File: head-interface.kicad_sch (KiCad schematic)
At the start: 10 parts, among them J1 NOZ, J2 FANS, J3 MOTOR_IN, J4 THERM, J5 HEATER, J6 PART_FAN, J7 FAN, J8 MOTOR

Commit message: rc1
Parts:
- H1, H2: symbol Mechanical:MountingHole -> Mechanical:MountingHole_Pad
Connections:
- new net GND: H1.1, H2.1
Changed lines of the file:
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@@
 (kicad_sch (version 20211123) (generator eeschema)
   (paper "A4")
+  (wire (pts (xy 139.7 83.82) (xy 139.7 81.28))
+    (stroke (width 0) (type default) (color 0 0 0 0))
+  )
   (wire (pts (xy 67.31 78.74) (xy 67.31 82.55))
     (stroke (width 0) (type default) (color 0 0 0 0))
@@
   )
   (wire (pts (xy 62.23 71.12) (xy 62.23 78.74))
+    (stroke (width 0) (type default) (color 0 0 0 0))
+  )
+  (wire (pts (xy 48.26 85.09) (xy 48.26 81.28))
     (stroke (width 0) (type default) (color 0 0 0 0))
   )
@@
     (pin "4")
   )
+  (symbol (lib_id "power:GND") (at 48.26 85.09 0) (unit 1)
+    (in_bom yes) (on_board yes) (fields_autoplaced)
+    (property "Reference" "#PWR?" (id 0) (at 48.26 91.44 0)
+      (effects (font (size 1.27 1.27)) hide)
+    )
+    (property "Value" "GND" (id 1) (at 48.26 90.17 0))
+    (property "Footprint" "" (id 2) (at 48.26 85.09 0)
+      (effects (font (size 1.27 1.27)) hide)
+    )
+    (property "Datasheet" "" (id 3) (at 48.26 85.09 0)
+      (effects (font (size 1.27 1.27)) hide)
+    )
+    (pin "1")
+  )
   (symbol (lib_id "Connector_Generic:Conn_01x04") (at 124.46 87.63 90) (mirror x) (unit 1)
     (in_bom yes) (on_board yes) (fields_autoplaced)
@@
     (pin "4")
   )
-  (symbol (lib_id "Mechanical:MountingHole") (at 50.8 77.47 0) (unit 1)
-    (in_bom yes) (on_board yes)
-    (property "Reference" "H1" (id 0) (at 53.34 76.1999 0)
-      (effects (font (size 1.27 1.27)) (justify left))
-    )
-    (property "Value" "MountingHole" (id 1) (at 44.45 81.28 0)
-      (effects (font (size 1.27 1.27)) (justify left))
-    )
-    (property "Footprint" "MountingHole:MountingHole_3.2mm_M3_Pad" (id 2) (at 50.8 77.47 0)
-      (effects (font (size 1.27 1.27)) hide)
-    )
-    (property "Datasheet" "~" (id 3) (at 50.8 77.47 0)
-      (effects (font (size 1.27 1.27)) hide)
-    )
+  (symbol (lib_id "power:GND") (at 139.7 83.82 0) (unit 1)
+    (in_bom yes) (on_board yes) (fields_autoplaced)
+    (property "Reference" "#PWR?" (id 0) (at 139.7 90.17 0)
+      (effects (font (size 1.27 1.27)) hide)
+    )
+    (property "Value" "GND" (id 1) (at 139.7 88.9 0))
+    (property "Footprint" "" (id 2) (at 139.7 83.82 0)
+      (effects (font (size 1.27 1.27)) hide)
+    )
+    (property "Datasheet" "" (id 3) (at 139.7 83.82 0)
+      (effects (font (size 1.27 1.27)) hide)
+    )
+    (pin "1")
+  )
+  (symbol (lib_id "Mechanical:MountingHole_Pad") (at 48.26 78.74 0) (unit 1)
+    (in_bom yes) (on_board yes)
+    (property "Reference" "H1" (id 0) (at 50.8 77.4699 0)
+      (effects (font (size 1.27 1.27)) (justify left))
+    )
+    (property "Value" "MountingHole" (id 1) (at 43.18 73.66 0)
+      (effects (font (size 1.27 1.27)) (justify left))
+    )
+    (property "Footprint" "MountingHole:MountingHole_3.2mm_M3_Pad" (id 2) (at 48.26 78.74 0)
+      (effects (font (size 1.27 1.27)) hide)
+    )
+    (property "Datasheet" "~" (id 3) (at 48.26 78.74 0)
+      (effects (font (size 1.27 1.27)) hide)
+    )
+    (pin "1")
   )
   (symbol (lib_id "Connector:Conn_01x04_Male") (at 124.46 66.04 90) (mirror x) (unit 1)
@@
     (pin "4")
   )
-  (symbol (lib_id "Mechanical:MountingHole") (at 138.43 76.2 0) (unit 1)
-    (in_bom yes) (on_board yes)
-    (property "Reference" "H2" (id 0) (at 140.97 74.9299 0)
-      (effects (font (size 1.27 1.27)) (justify left))
-    )
-    (property "Value" "MountingHole" (id 1) (at 134.62 80.01 0)
-      (effects (font (size 1.27 1.27)) (justify left))
-    )
-    (property "Footprint" "MountingHole:MountingHole_3.2mm_M3_Pad" (id 2) (at 138.43 76.2 0)
-      (effects (font (size 1.27 1.27)) hide)
-    )
-    (property "Datasheet" "~" (id 3) (at 138.43 76.2 0)
-      (effects (font (size 1.27 1.27)) hide)
-    )
+  (symbol (lib_id "Mechanical:MountingHole_Pad") (at 139.7 78.74 0) (unit 1)
+    (in_bom yes) (on_board yes)
+    (property "Reference" "H2" (id 0) (at 142.24 77.4699 0)
+      (effects (font (size 1.27 1.27)) (justify left))
+    )
+    (property "Value" "MountingHole" (id 1) (at 134.62 73.66 0)
+      (effects (font (size 1.27 1.27)) (justify left))
+    )
+    (property "Footprint" "MountingHole:MountingHole_3.2mm_M3_Pad" (id 2) (at 139.7 78.74 0)
+      (effects (font (size 1.27 1.27)) hide)
+    )
+    (property "Datasheet" "~" (id 3) (at 139.7 78.74 0)
+      (effects (font (size 1.27 1.27)) hide)
+    )
+    (pin "1")
   )
   (sheet_instances
@@
   )
   (symbol_instances
+    (path "/41940eff-de59-41c7-a4cb-1d5162f88769"
+      (reference "#PWR?") (unit 1) (value "GND") (footprint "")
+    )
+    (path "/86958ac6-442c-4e3e-8dcd-11b806cba16b"
+      (reference "#PWR?") (unit 1) (value "GND") (footprint "")
+    )
     (path "/8e52f6d5-b989-4f08-bbd8-4578e3ffd601"
       (reference "H1") (unit 1) (value "MountingHole") (footprint "MountingHole:MountingHole_3.2mm_M3_Pad")

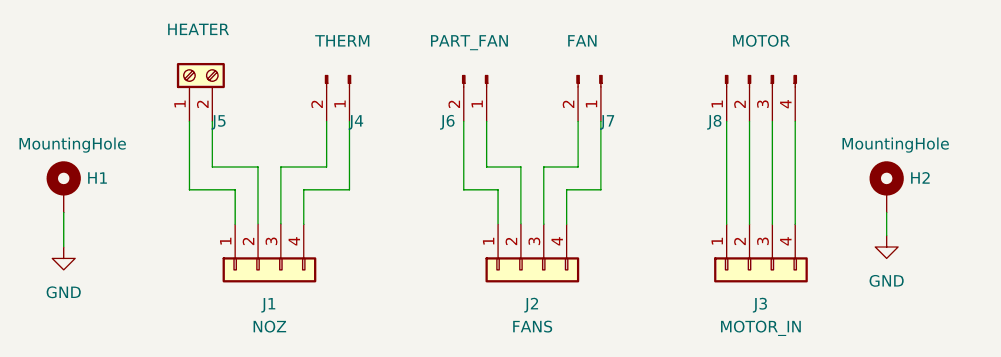
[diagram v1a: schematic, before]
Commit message: added 2nd part fan connector
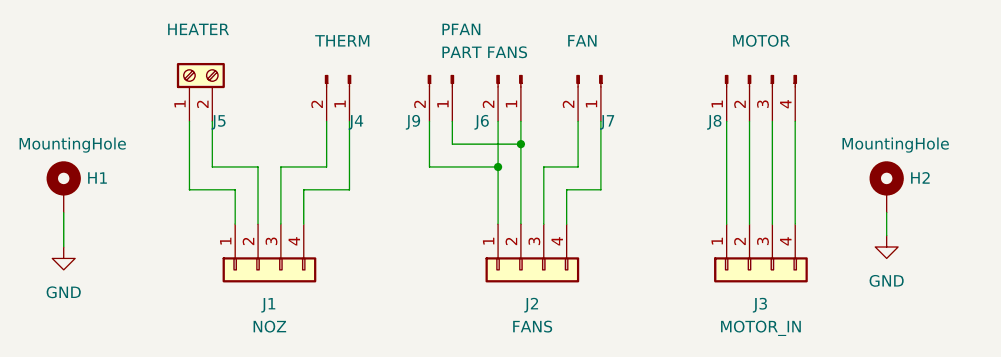
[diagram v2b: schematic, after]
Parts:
- added J9: PFAN, Connector_JST:JST_PH_B2B-PH-K_1x02_P2.00mm_Vertical, symbol Connector:Conn_01x02_Male
- J6: value PART_FAN -> PART FANS
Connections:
- net at J2.2 (Pin_2), J6.1 (Pin_1): now also J9.1 (Pin_1)
- net at J2.1 (Pin_1), J6.2 (Pin_2): now also J9.2 (Pin_2)
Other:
- moved on the sheet: J6
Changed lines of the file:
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@@
 (kicad_sch (version 20211123) (generator eeschema)
   (paper "A4")
+  (junction (at 99.06 73.66) (diameter 0) (color 0 0 0 0)
+  )
+  (junction (at 96.52 76.2) (diameter 0) (color 0 0 0 0)
+  )
   (wire (pts (xy 139.7 83.82) (xy 139.7 81.28))
     (stroke (width 0) (type default) (color 0 0 0 0))
@@
     (stroke (width 0) (type default) (color 0 0 0 0))
   )
+  (wire (pts (xy 99.06 73.66) (xy 99.06 82.55))
+    (stroke (width 0) (type default) (color 0 0 0 0))
+  )
+  (wire (pts (xy 91.44 71.12) (xy 91.44 73.66))
+    (stroke (width 0) (type default) (color 0 0 0 0))
+  )
   (wire (pts (xy 105.41 76.2) (xy 101.6 76.2))
     (stroke (width 0) (type default) (color 0 0 0 0))
   )
-  (wire (pts (xy 95.25 71.12) (xy 95.25 76.2))
-    (stroke (width 0) (type default) (color 0 0 0 0))
-  )
   (wire (pts (xy 101.6 76.2) (xy 101.6 82.55))
     (stroke (width 0) (type default) (color 0 0 0 0))
@@
     (stroke (width 0) (type default) (color 0 0 0 0))
   )
-  (wire (pts (xy 92.71 78.74) (xy 92.71 71.12))
-    (stroke (width 0) (type default) (color 0 0 0 0))
-  )
   (wire (pts (xy 121.92 82.55) (xy 121.92 71.12))
     (stroke (width 0) (type default) (color 0 0 0 0))
@@
     (stroke (width 0) (type default) (color 0 0 0 0))
   )
-  (wire (pts (xy 96.52 78.74) (xy 92.71 78.74))
-    (stroke (width 0) (type default) (color 0 0 0 0))
-  )
   (wire (pts (xy 127 82.55) (xy 127 71.12))
     (stroke (width 0) (type default) (color 0 0 0 0))
@@
     (stroke (width 0) (type default) (color 0 0 0 0))
   )
+  (wire (pts (xy 88.9 71.12) (xy 88.9 76.2))
+    (stroke (width 0) (type default) (color 0 0 0 0))
+  )
   (wire (pts (xy 48.26 85.09) (xy 48.26 81.28))
     (stroke (width 0) (type default) (color 0 0 0 0))
   )
-  (wire (pts (xy 95.25 76.2) (xy 99.06 76.2))
-    (stroke (width 0) (type default) (color 0 0 0 0))
-  )
-  (wire (pts (xy 99.06 76.2) (xy 99.06 82.55))
-    (stroke (width 0) (type default) (color 0 0 0 0))
-  )
-  (wire (pts (xy 96.52 82.55) (xy 96.52 78.74))
+  (wire (pts (xy 88.9 76.2) (xy 96.52 76.2))
+    (stroke (width 0) (type default) (color 0 0 0 0))
+  )
+  (wire (pts (xy 99.06 71.12) (xy 99.06 73.66))
+    (stroke (width 0) (type default) (color 0 0 0 0))
+  )
+  (wire (pts (xy 96.52 76.2) (xy 96.52 71.12))
+    (stroke (width 0) (type default) (color 0 0 0 0))
+  )
+  (wire (pts (xy 96.52 82.55) (xy 96.52 76.2))
     (stroke (width 0) (type default) (color 0 0 0 0))
   )
@@
   )
   (wire (pts (xy 69.85 76.2) (xy 69.85 82.55))
+    (stroke (width 0) (type default) (color 0 0 0 0))
+  )
+  (wire (pts (xy 91.44 73.66) (xy 99.06 73.66))
     (stroke (width 0) (type default) (color 0 0 0 0))
   )
@@
     (pin "4")
   )
+  (symbol (lib_id "Connector:Conn_01x02_Male") (at 91.44 66.04 270) (unit 1)
+    (in_bom yes) (on_board yes)
+    (property "Reference" "J9" (id 0) (at 86.36 71.12 90)
+      (effects (font (size 1.27 1.27)) (justify left))
+    )
+    (property "Value" "PFAN" (id 1) (at 90.17 60.96 90)
+      (effects (font (size 1.27 1.27)) (justify left))
+    )
+    (property "Footprint" "Connector_JST:JST_PH_B2B-PH-K_1x02_P2.00mm_Vertical" (id 2) (at 91.44 66.04 0)
+      (effects (font (size 1.27 1.27)) hide)
+    )
+    (property "Datasheet" "~" (id 3) (at 91.44 66.04 0)
+      (effects (font (size 1.27 1.27)) hide)
+    )
+    (pin "1")
+    (pin "2")
+  )
   (symbol (lib_id "power:GND") (at 48.26 85.09 0) (unit 1)
     (in_bom yes) (on_board yes) (fields_autoplaced)
-    (property "Reference" "#PWR?" (id 0) (at 48.26 91.44 0)
+    (property "Reference" "#PWR0102" (id 0) (at 48.26 91.44 0)
       (effects (font (size 1.27 1.27)) hide)
     )
@@
   (symbol (lib_id "power:GND") (at 139.7 83.82 0) (unit 1)
     (in_bom yes) (on_board yes) (fields_autoplaced)
-    (property "Reference" "#PWR?" (id 0) (at 139.7 90.17 0)
+    (property "Reference" "#PWR0101" (id 0) (at 139.7 90.17 0)
       (effects (font (size 1.27 1.27)) hide)
     )
@@
     (pin "2")
   )
-  (symbol (lib_id "Connector:Conn_01x02_Male") (at 95.25 66.04 270) (unit 1)
-    (in_bom yes) (on_board yes)
-    (property "Reference" "J6" (id 0) (at 90.17 71.12 90)
-      (effects (font (size 1.27 1.27)) (justify left))
-    )
-    (property "Value" "PART_FAN" (id 1) (at 88.9 62.23 90)
-      (effects (font (size 1.27 1.27)) (justify left))
-    )
-    (property "Footprint" "Connector_JST:JST_PH_B2B-PH-K_1x02_P2.00mm_Vertical" (id 2) (at 95.25 66.04 0)
-      (effects (font (size 1.27 1.27)) hide)
-    )
-    (property "Datasheet" "~" (id 3) (at 95.25 66.04 0)
+  (symbol (lib_id "Connector:Conn_01x02_Male") (at 99.06 66.04 270) (unit 1)
+    (in_bom yes) (on_board yes)
+    (property "Reference" "J6" (id 0) (at 93.98 71.12 90)
+      (effects (font (size 1.27 1.27)) (justify left))
+    )
+    (property "Value" "PART FANS" (id 1) (at 90.17 63.5 90)
+      (effects (font (size 1.27 1.27)) (justify left))
+    )
+    (property "Footprint" "Connector_JST:JST_PH_B2B-PH-K_1x02_P2.00mm_Vertical" (id 2) (at 99.06 66.04 0)
+      (effects (font (size 1.27 1.27)) hide)
+    )
+    (property "Datasheet" "~" (id 3) (at 99.06 66.04 0)
       (effects (font (size 1.27 1.27)) hide)
     )
@@
   )
   (symbol_instances
+    (path "/86958ac6-442c-4e3e-8dcd-11b806cba16b"
+      (reference "#PWR0101") (unit 1) (value "GND") (footprint "")
+    )
     (path "/41940eff-de59-41c7-a4cb-1d5162f88769"
-      (reference "#PWR?") (unit 1) (value "GND") (footprint "")
-    )
-    (path "/86958ac6-442c-4e3e-8dcd-11b806cba16b"
-      (reference "#PWR?") (unit 1) (value "GND") (footprint "")
+      (reference "#PWR0102") (unit 1) (value "GND") (footprint "")
     )
     (path "/8e52f6d5-b989-4f08-bbd8-4578e3ffd601"
@@
     )
     (path "/a6be91b6-07f6-4542-b463-84d0ca113071"
-      (reference "J6") (unit 1) (value "PART_FAN") (footprint "Connector_JST:JST_PH_B2B-PH-K_1x02_P2.00mm_Vertical")
+      (reference "J6") (unit 1) (value "PART FANS") (footprint "Connector_JST:JST_PH_B2B-PH-K_1x02_P2.00mm_Vertical")
     )
     (path "/07730fe3-b9f7-4c44-9625-7fa0966285d1"
@@
       (reference "J8") (unit 1) (value "MOTOR") (footprint "Connector_JST:JST_EH_B4B-EH-A_1x04_P2.50mm_Vertical")
     )
-  )
+    (path "/3f9f80dd-199d-41a9-a918-456286fc49ff"
+      (reference "J9") (unit 1) (value "PFAN") (footprint "Connector_JST:JST_PH_B2B-PH-K_1x02_P2.00mm_Vertical")
+    )
+  )
